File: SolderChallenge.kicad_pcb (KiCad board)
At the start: 2 copper layers, 50 x 100 mm, 41 parts, among them Q1 MOS_N, Q2 MOS_N, Q3 MOS_N, Q4 MOS_N_x2, U1 555, U2 555, U3 555

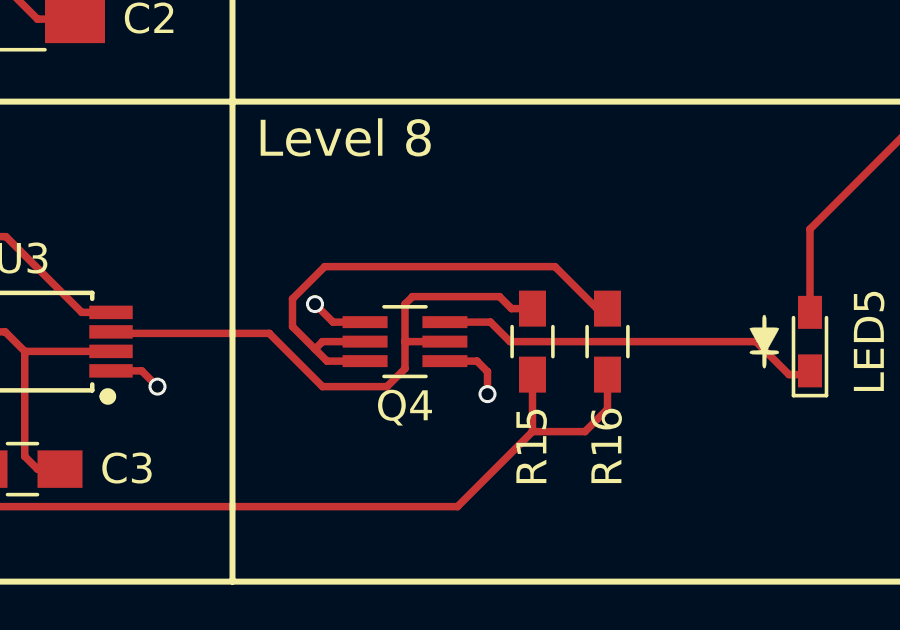
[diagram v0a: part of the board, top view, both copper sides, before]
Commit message: Decrease pad length on Q4, SOT-666. Long pads made it harder to align
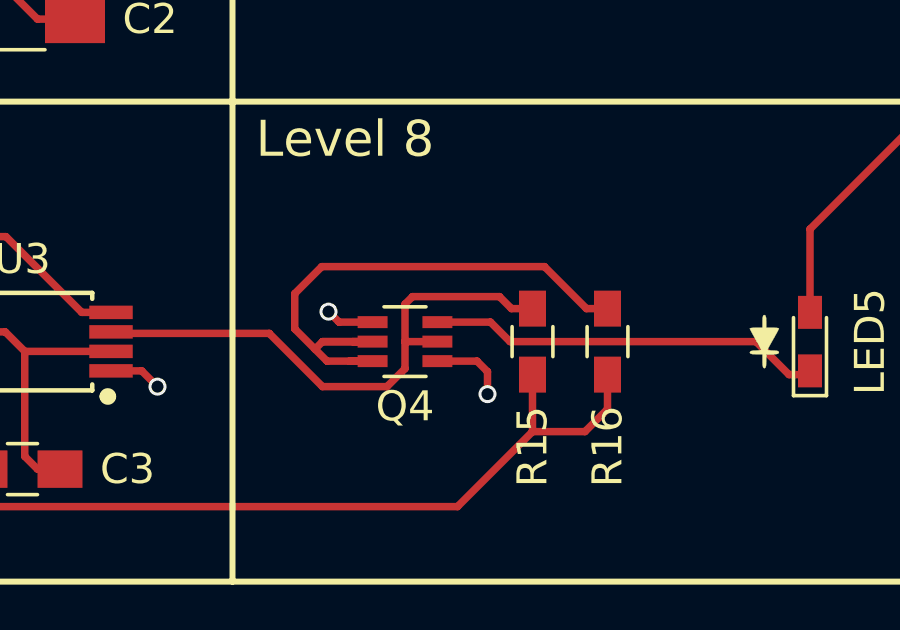
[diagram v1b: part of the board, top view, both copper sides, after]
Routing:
- net Net-(Q4-Pad2): track 18.8 -> 20.5 mm
- net GND: track 38.3 -> 37.6 mm
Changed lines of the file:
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@@
     (add_net VCC)
+  )
+  (module SolderChallenge:SOT-363_SC-70-6_Handsoldering (layer F.Cu)
+    (at 80.75 132)
+    (descr "SOT-363, SC-70-6, Handsoldering")
+    (attr smd)
+    (fp_text reference Q4 (at 0 2.159) (layer F.SilkS)
+      (effects (font (size 1 1) (thickness 0.15)))
+    )
+    (fp_text value MOS_N_x2 (at 0 -2.2606) (layer F.Fab) hide
+      (effects (font (size 1 1) (thickness 0.15)))
+    )
+    (fp_line (start -0.175 -1.1) (end -0.675 -0.6) (layer F.Fab) (width 0.1))
+    (fp_line (start 0.675 1.1) (end -0.675 1.1) (layer F.Fab) (width 0.1))
+    (fp_line (start 0.675 -1.1) (end 0.675 1.1) (layer F.Fab) (width 0.1))
+    (fp_line (start -0.675 -0.6) (end -0.675 1.1) (layer F.Fab) (width 0.1))
+    (fp_line (start 0.675 -1.1) (end -0.175 -1.1) (layer F.Fab) (width 0.1))
+    (fp_line (start -2.4 -1.4) (end 2.4 -1.4) (layer F.CrtYd) (width 0.05))
+    (fp_line (start -2.4 -1.4) (end -2.4 1.4) (layer F.CrtYd) (width 0.05))
+    (fp_line (start 2.4 1.4) (end 2.4 -1.4) (layer F.CrtYd) (width 0.05))
+    (fp_line (start -0.7 1.16) (end 0.7 1.16) (layer F.SilkS) (width 0.12))
+    (fp_line (start 0.7 -1.16) (end -0.7 -1.16) (layer F.SilkS) (width 0.12))
+    (fp_line (start -2.4 1.4) (end 2.4 1.4) (layer F.CrtYd) (width 0.05))
+    (pad 7 connect circle (at -1.2954 -1.4986) (size 0.5 0.5) (layers F.SilkS))
+    (pad 6 smd rect (at 1.08 -0.65) (size 1 0.4) (layers F.Cu F.Paste F.Mask)
+      (net 14 "Net-(LED5-Pad1)"))
+    (pad 5 smd rect (at 1.08 0) (size 1 0.4) (layers F.Cu F.Paste F.Mask)
+      (net 17 "Net-(Q4-Pad5)"))
+    (pad 4 smd rect (at 1.08 0.65) (size 1 0.4) (layers F.Cu F.Paste F.Mask)
+      (net 2 GND))
+    (pad 3 smd rect (at -1.08 0.65) (size 1 0.4) (layers F.Cu F.Paste F.Mask)
+      (net 16 "Net-(Q4-Pad2)"))
+    (pad 2 smd rect (at -1.08 0) (size 1 0.4) (layers F.Cu F.Paste F.Mask)
+      (net 16 "Net-(Q4-Pad2)"))
+    (pad 1 smd rect (at -1.08 -0.65) (size 1 0.4) (layers F.Cu F.Paste F.Mask)
+      (net 2 GND))
+    (model TO_SOT_Packages_SMD.3dshapes/SC-70-6.wrl
+      (at (xyz 0 0 0))
+      (scale (xyz 1 1 1))
+      (rotate (xyz 0 0 0))
+    )
   )
   (module SolderChallenge:SOT-23_GSD_Handsoldering (layer F.Cu)
@@
       (xy 0.296333 -0.275166) (xy 0.304643 -0.400728) (xy 0.3329 -0.457921) (xy 0.359833 -0.465666)
       (xy 0.399766 -0.443007)) (layer F.SilkS) (width 0.01))
-  )
-  (module SolderChallenge:SOT-363_SC-70-6_Handsoldering (layer F.Cu)
-    (at 80.75 132)
-    (descr "SOT-363, SC-70-6, Handsoldering")
-    (attr smd)
-    (fp_text reference Q4 (at 0 2.159) (layer F.SilkS)
-      (effects (font (size 1 1) (thickness 0.15)))
-    )
-    (fp_text value MOS_N_x2 (at 0 -2.2606) (layer F.Fab) hide
-      (effects (font (size 1 1) (thickness 0.15)))
-    )
-    (fp_line (start -2.4 1.4) (end 2.4 1.4) (layer F.CrtYd) (width 0.05))
-    (fp_line (start 0.7 -1.16) (end -0.7 -1.16) (layer F.SilkS) (width 0.12))
-    (fp_line (start -0.7 1.16) (end 0.7 1.16) (layer F.SilkS) (width 0.12))
-    (fp_line (start 2.4 1.4) (end 2.4 -1.4) (layer F.CrtYd) (width 0.05))
-    (fp_line (start -2.4 -1.4) (end -2.4 1.4) (layer F.CrtYd) (width 0.05))
-    (fp_line (start -2.4 -1.4) (end 2.4 -1.4) (layer F.CrtYd) (width 0.05))
-    (fp_line (start 0.675 -1.1) (end -0.175 -1.1) (layer F.Fab) (width 0.1))
-    (fp_line (start -0.675 -0.6) (end -0.675 1.1) (layer F.Fab) (width 0.1))
-    (fp_line (start 0.675 -1.1) (end 0.675 1.1) (layer F.Fab) (width 0.1))
-    (fp_line (start 0.675 1.1) (end -0.675 1.1) (layer F.Fab) (width 0.1))
-    (fp_line (start -0.175 -1.1) (end -0.675 -0.6) (layer F.Fab) (width 0.1))
-    (pad 1 smd rect (at -1.33 -0.65) (size 1.5 0.4) (layers F.Cu F.Paste F.Mask)
-      (net 2 GND))
-    (pad 2 smd rect (at -1.33 0) (size 1.5 0.4) (layers F.Cu F.Paste F.Mask)
-      (net 16 "Net-(Q4-Pad2)"))
-    (pad 3 smd rect (at -1.33 0.65) (size 1.5 0.4) (layers F.Cu F.Paste F.Mask)
-      (net 16 "Net-(Q4-Pad2)"))
-    (pad 4 smd rect (at 1.33 0.65) (size 1.5 0.4) (layers F.Cu F.Paste F.Mask)
-      (net 2 GND))
-    (pad 5 smd rect (at 1.33 0) (size 1.5 0.4) (layers F.Cu F.Paste F.Mask)
-      (net 17 "Net-(Q4-Pad5)"))
-    (pad 6 smd rect (at 1.33 -0.65) (size 1.5 0.4) (layers F.Cu F.Paste F.Mask)
-      (net 14 "Net-(LED5-Pad1)"))
-    (pad 7 connect circle (at -1.2954 -1.4986) (size 0.5 0.5) (layers F.SilkS))
-    (model TO_SOT_Packages_SMD.3dshapes/SC-70-6.wrl
-      (at (xyz 0 0 0))
-      (scale (xyz 1 1 1))
-      (rotate (xyz 0 0 0))
-    )
   )
   (module SolderChallenge:PointsTime_writing (layer F.Cu)
@@
   (segment (start 83.15 132.65) (end 83.5 133) (width 0.25) (layer F.Cu) (net 2))
   (segment (start 83.5 133) (end 83.5 133.75) (width 0.25) (layer F.Cu) (net 2))
-  (segment (start 79.42 131.35) (end 78.35 131.35) (width 0.25) (layer F.Cu) (net 2))
-  (segment (start 78.35 131.35) (end 77.75 130.75) (width 0.25) (layer F.Cu) (net 2))
-  (via (at 77.75 130.75) (size 0.6) (drill 0.4) (layers F.Cu B.Cu) (net 2))
-  (segment (start 79.42 131.35) (end 79.1 131.35) (width 0.25) (layer F.Cu) (net 2))
   (via (at 83.5 133.75) (size 0.6) (drill 0.4) (layers F.Cu B.Cu) (net 2))
   (segment (start 65.25 136.25) (end 65.25 130.75) (width 0.25) (layer B.Cu) (net 2))
@@
   (segment (start 87.45 116.75) (end 87.45 118.25) (width 0.25) (layer F.Cu) (net 2))
   (segment (start 87.45 118.25) (end 87.5 118.3) (width 0.25) (layer F.Cu) (net 2))
+  (via (at 78.2 131) (size 0.6) (drill 0.4) (layers F.Cu B.Cu) (net 2))
+  (segment (start 78.55 131.35) (end 79.67 131.35) (width 0.25) (layer F.Cu) (net 2))
+  (segment (start 78.2 131) (end 78.55 131.35) (width 0.25) (layer F.Cu) (net 2))
   (segment (start 59.08 98.72) (end 61.62 101.26) (width 0.25) (layer B.Cu) (net 3))
   (segment (start 61.62 101.26) (end 66.7 101.26) (width 0.25) (layer B.Cu) (net 3))
@@
   (segment (start 94.25 128.25) (end 94.25 130.9) (width 0.25) (layer F.Cu) (net 15))
   (segment (start 97.5 125) (end 94.25 128.25) (width 0.25) (layer F.Cu) (net 15))
-  (segment (start 77.75 132.25) (end 77 131.5) (width 0.25) (layer F.Cu) (net 16))
-  (segment (start 77 131.5) (end 77 130.574998) (width 0.25) (layer F.Cu) (net 16))
-  (segment (start 85.75 129.5) (end 87.15 130.9) (width 0.25) (layer F.Cu) (net 16))
-  (segment (start 77 130.574998) (end 78.074998 129.5) (width 0.25) (layer F.Cu) (net 16))
-  (segment (start 78.074998 129.5) (end 85.75 129.5) (width 0.25) (layer F.Cu) (net 16))
-  (segment (start 87.15 130.9) (end 87.5 130.9) (width 0.25) (layer F.Cu) (net 16))
   (segment (start 77.75 132.25) (end 78 132) (width 0.25) (layer F.Cu) (net 16))
   (segment (start 78 132) (end 79.42 132) (width 0.25) (layer F.Cu) (net 16))
@@
   (segment (start 79.8 132.65) (end 78.9 132.65) (width 0.25) (layer F.Cu) (net 16))
   (segment (start 79 132) (end 79.8 132) (width 0.25) (layer F.Cu) (net 16))
+  (segment (start 77.074998 130.399998) (end 77.974996 129.5) (width 0.25) (layer F.Cu) (net 16))
+  (segment (start 85.4 129.5) (end 86.8 130.9) (width 0.25) (layer F.Cu) (net 16))
+  (segment (start 86.8 130.9) (end 87.5 130.9) (width 0.25) (layer F.Cu) (net 16))
+  (segment (start 77.074998 131.574998) (end 77.074998 130.399998) (width 0.25) (layer F.Cu) (net 16))
+  (segment (start 77.75 132.25) (end 77.074998 131.574998) (width 0.25) (layer F.Cu) (net 16))
+  (segment (start 77.974996 129.5) (end 85.4 129.5) (width 0.25) (layer F.Cu) (net 16))
+  (segment (start 79.67 132) (end 78 132) (width 0.25) (layer F.Cu) (net 16))
   (segment (start 80.75 132) (end 80.75 132.900002) (width 0.25) (layer F.Cu) (net 17))
   (segment (start 80.75 132.900002) (end 80.150002 133.5) (width 0.25) (layer F.Cu) (net 17))

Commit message: Added a name box on back silkscreen
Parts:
- added G***: LOGO, SolderChallenge:Name_Box, B.Cu at (75.1, 145.3)
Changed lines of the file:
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@@
     (tracks 256)
     (zones 0)
-    (modules 41)
+    (modules 42)
     (nets 27)
   )
@@
     )
   )
+  (module SolderChallenge:Name_Box (layer B.Cu)
+    (at 75.1 145.3)
+    (fp_text reference G*** (at 0 0) (layer B.SilkS) hide
+      (effects (font (size 1.524 1.524) (thickness 0.3)) (justify mirror))
+    )
+    (fp_text value LOGO (at 0.75 0) (layer B.SilkS) hide
+      (effects (font (size 1.524 1.524) (thickness 0.3)) (justify mirror))
+    )
+    (fp_poly (pts (xy 19.539034 2.348381) (xy 19.739442 2.184492) (xy 19.874381 2.013034) (xy 20.0025 1.805806)
+      (xy 20.0025 -1.8415) (xy 19.88876 -2.034971) (xy 19.728652 -2.237264) (xy 19.519655 -2.400393)
+      (xy 19.300595 -2.498643) (xy 19.245648 -2.502217) (xy 19.106764 -2.50563) (xy 18.884674 -2.508883)
+      (xy 18.580106 -2.511974) (xy 18.19379 -2.5149) (xy 17.726456 -2.517661) (xy 17.178834 -2.520255)
+      (xy 16.551654 -2.522681) (xy 15.845644 -2.524937) (xy 15.061536 -2.527021) (xy 14.200058 -2.528933)
+      (xy 13.26194 -2.53067) (xy 12.247913 -2.532232) (xy 11.158705 -2.533616) (xy 9.995046 -2.534821)
+      (xy 8.757667 -2.535846) (xy 7.447296 -2.536689) (xy 6.064664 -2.537349) (xy 4.610501 -2.537823)
+      (xy 3.085535 -2.538112) (xy 1.490497 -2.538213) (xy 0.000279 -2.538142) (xy -1.563296 -2.537953)
+      (xy -3.044259 -2.537692) (xy -4.444663 -2.537355) (xy -5.766563 -2.536934) (xy -7.012012 -2.536424)
+      (xy -8.183065 -2.535819) (xy -9.281776 -2.535113) (xy -10.310199 -2.5343) (xy -11.270387 -2.533373)
+      (xy -12.164396 -2.532328) (xy -12.994278 -2.531157) (xy -13.762089 -2.529854) (xy -14.469882 -2.528415)
+      (xy -15.119711 -2.526832) (xy -15.71363 -2.5251) (xy -16.253694 -2.523212) (xy -16.741955 -2.521164)
+      (xy -17.18047 -2.518948) (xy -17.571291 -2.516558) (xy -17.916473 -2.513989) (xy -18.218069 -2.511235)
+      (xy -18.478134 -2.508289) (xy -18.698722 -2.505146) (xy -18.881886 -2.5018) (xy -19.029682 -2.498244)
+      (xy -19.144162 -2.494472) (xy -19.227382 -2.490479) (xy -19.281395 -2.486259) (xy -19.308255 -2.481805)
+      (xy -19.308865 -2.481596) (xy -19.564057 -2.35103) (xy -19.763525 -2.158648) (xy -19.843587 -2.039817)
+      (xy -19.960167 -1.8415) (xy -19.960167 1.805806) (xy -19.832048 2.013034) (xy -19.668159 2.213442)
+      (xy -19.496701 2.348381) (xy -19.289473 2.4765) (xy 19.331806 2.4765) (xy 19.539034 2.348381)) (layer B.SilkS) (width 0.01))
+  )
   (gr_line (start 92.7 102.9) (end 92.1 102.2) (layer F.SilkS) (width 0.15))

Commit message: Add 'JLCJLCJLCJLC' placement to allow JLCPCB to place order number at right place on board
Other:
- board text added: "JLCJLCJLCJLC"
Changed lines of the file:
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@@
   (general
     (thickness 1.6)
-    (drawings 58)
+    (drawings 59)
     (tracks 256)
     (zones 0)
@@
     (47 F.CrtYd user)
     (48 B.Fab user)
-    (49 F.Fab user hide)
+    (49 F.Fab user)
   )
   (setup
@@
       (xy -19.496701 2.348381) (xy -19.289473 2.4765) (xy 19.331806 2.4765) (xy 19.539034 2.348381)) (layer B.SilkS) (width 0.01))
   )
+  (gr_text JLCJLCJLCJLC (at 90.2 86 90) (layer B.Fab)
+    (effects (font (size 0.8 0.8) (thickness 0.15)))
+  )
   (gr_line (start 92.7 102.9) (end 92.1 102.2) (layer F.SilkS) (width 0.15))
